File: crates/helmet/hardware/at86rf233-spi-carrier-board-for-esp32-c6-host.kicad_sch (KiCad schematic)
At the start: 23 parts, among them J1 Conn_01x09, U1 AT86RF233-ZU, Y1 16MHz

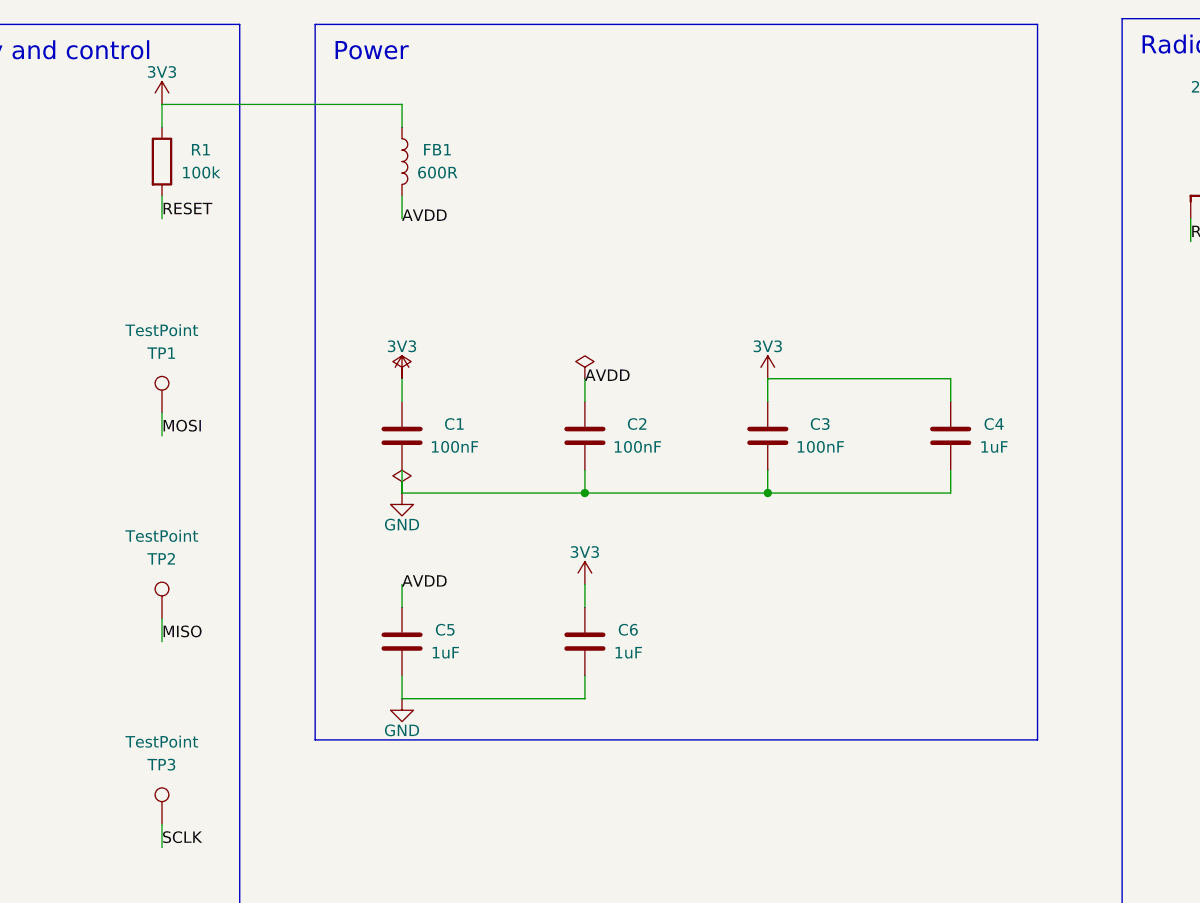
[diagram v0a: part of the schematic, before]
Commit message: copperhead: create pipeline stage: schematic
Created the BOM-consistent AT86RF233 carrier schematic and PINOUT.md. Symbol verification and ERC are clean; legibility has 0 errors and drift is clean.

Verification: ERC clean
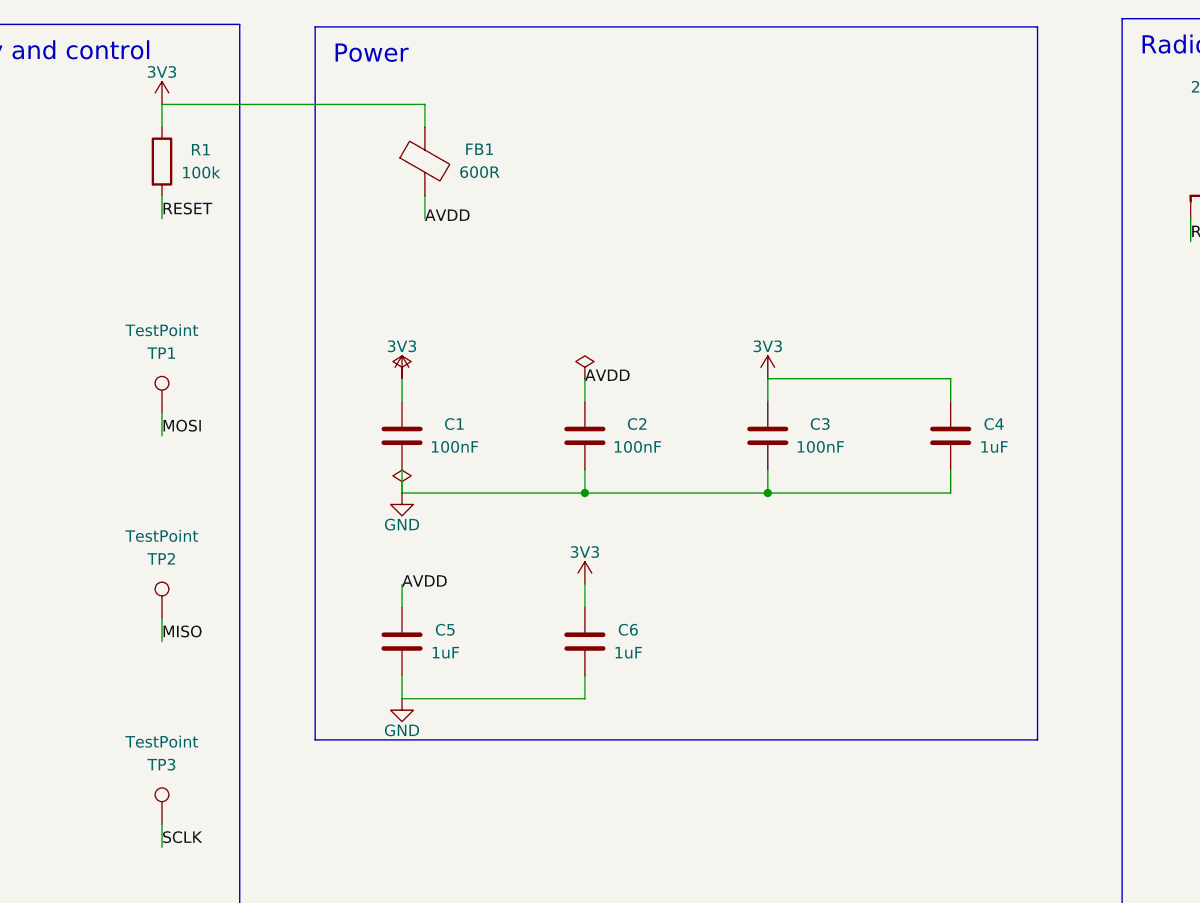
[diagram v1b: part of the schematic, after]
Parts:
- FB1: symbol Device:L -> Device:FerriteBead
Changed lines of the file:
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@@
 	)
 	(wire
-		(pts (xy 134.62 90.17) (xy 134.62 87.63))
-		(stroke (width 0) (type default))
-	)
-	(wire
-		(pts (xy 107.95 87.63) (xy 134.62 87.63))
+		(pts (xy 137.16 90.17) (xy 137.16 87.63))
+		(stroke (width 0) (type default))
+	)
+	(wire
+		(pts (xy 107.95 87.63) (xy 137.16 87.63))
 		(stroke (width 0) (type default))
 	)
@@
 	)
 	(wire
-		(pts (xy 134.62 97.79) (xy 134.62 100.33))
+		(pts (xy 137.16 97.79) (xy 137.16 100.33))
 		(stroke (width 0) (type default))
 	)
@@
 		(fill (type none))
 	)
-	(rectangle (start 124.968 78.74) (end 205.232 158.242)
+	(rectangle (start 124.968 79.0194) (end 205.232 158.242)
 		(stroke (width 0.152) (type solid))
 		(fill (type none))
@@
 		(effects (font (size 2 2)) (justify left top))
 	)
-	(text "Power" (at 126.968 80.74 0)
+	(text "Power" (at 126.968 81.0194 0)
 		(effects (font (size 2 2)) (justify left top))
 	)
@@
 		(effects (font (size 1.27 1.27)))
 	)
-	(label "AVDD" (at 134.62 100.33 0)
+	(label "AVDD" (at 137.16 100.33 0)
 		(effects (font (size 1.27 1.27)))
 	)
@@
 	)
 	(symbol
-		(lib_id "Device:L")
-		(at 134.62 93.98 0)
-		(unit 1)
-		(exclude_from_sim no)
-		(in_bom yes)
-		(on_board yes)
-		(dnp no)
-		(property "Reference" "FB1" (at 138.5543 92.71 0)
-			(effects (font (size 1.27 1.27)))
-		)
-		(property "Value" "600R" (at 138.5543 95.25 0)
-			(effects (font (size 1.27 1.27)))
-		)
-		(property "Footprint" "Inductor_SMD:L_0402_1005Metric" (at 134.62 93.98 0)
-			(effects (font (size 1.27 1.27)) hide)
-		)
-		(property "Datasheet" "~" (at 134.62 93.98 0)
-			(effects (font (size 1.27 1.27)) hide)
-		)
+		(lib_id "Device:FerriteBead")
+		(at 137.16 93.98 0)
+		(unit 1)
+		(exclude_from_sim no)
+		(in_bom yes)
+		(on_board yes)
+		(dnp no)
+		(property "Reference" "FB1" (at 143.2306 92.6592 0)
+			(effects (font (size 1.27 1.27)))
+		)
+		(property "Value" "600R" (at 143.2306 95.1992 0)
+			(effects (font (size 1.27 1.27)))
+		)
+		(property "Footprint" "Inductor_SMD:L_0402_1005Metric" (at 137.16 93.98 0)
+			(effects (font (size 1.27 1.27)) hide)
+		)
+		(property "Datasheet" "~" (at 137.16 93.98 0)
+			(effects (font (size 1.27 1.27)) hide)
+		)

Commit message: prepare AT86RF233 carrier for PCB layout
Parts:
- AE1: footprint Antenna:Antennas_Chip_2.4GHz -> RF_Antenna:Johanson_2450AT18x100
- TP1, TP2, TP3, TP4, TP5: footprint Connector_PinHeader_1.00mm:PinHeader_1x01_P1.00mm_Vertical -> TestPoint:TestPoint_Keystone_5015_Micro_Mini
- U1: footprint Package_DFN_QFN:QFN-32-1EP_5x5mm_P0.5mm_EP3.35x3.35mm -> Package_DFN_QFN:QFN-32-1EP_5x5mm_P0.5mm_EP3.3x3.3mm
- Y1: footprint Crystal:Crystal_SMD_3225-4Pin_3.2x2.5mm -> Crystal:Crystal_SMD_Abracon_ABM8G-4Pin_3.2x2.5mm
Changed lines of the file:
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@@
 	)
 	(symbol
-		(lib_id "power:PWR_FLAG")
+		(lib_id "copperhead_power:PWR_FLAG")
 		(at 134.62 118.11 0)
 		(unit 1)
@@
 	)
 	(symbol
-		(lib_id "power:PWR_FLAG")
+		(lib_id "copperhead_power:PWR_FLAG")
 		(at 154.94 118.11 0)
 		(unit 1)
@@
 	)
 	(symbol
-		(lib_id "power:PWR_FLAG")
+		(lib_id "copperhead_power:PWR_FLAG")
 		(at 134.62 130.81 0)
 		(unit 1)
@@
 	)
 	(symbol
-		(lib_id "power:+3V3")
+		(lib_id "copperhead_power:3V3")
 		(at 107.95 87.63 0)
 		(unit 1)
@@
 	)
 	(symbol
-		(lib_id "power:+3V3")
+		(lib_id "copperhead_power:3V3")
 		(at 175.26 118.11 0)
 		(unit 1)
@@
 	)
 	(symbol
-		(lib_id "power:+3V3")
+		(lib_id "copperhead_power:3V3")
 		(at 134.62 118.11 0)
 		(unit 1)
@@
 	)
 	(symbol
-		(lib_id "power:+3V3")
+		(lib_id "copperhead_power:3V3")
 		(at 154.94 140.97 0)
 		(unit 1)
@@
 	)
 	(symbol
-		(lib_id "power:+3V3")
+		(lib_id "copperhead_power:3V3")
 		(at 69.85 92.71 0)
 		(unit 1)
@@
 	)
 	(symbol
-		(lib_id "power:+3V3")
+		(lib_id "copperhead_power:3V3")
 		(at 303.53 111.76 0)
 		(unit 1)
@@
 	)
 	(symbol
-		(lib_id "power:+3V3")
+		(lib_id "copperhead_power:3V3")
 		(at 295.91 111.76 0)
 		(unit 1)
@@
 		)
 	)
-	(label "AVDD" (at 154.94 118.11 0)
-		(effects (font (size 1.27 1.27)))
-	)
-	(label "AVDD" (at 134.62 140.97 0)
-		(effects (font (size 1.27 1.27)))
-	)
-	(label "AVDD" (at 137.16 100.33 0)
-		(effects (font (size 1.27 1.27)))
-	)
-	(label "AVDD" (at 300.99 109.22 0)
-		(effects (font (size 1.27 1.27)))
-	)
-	(symbol
-		(lib_id "power:GND")
+	(symbol
+		(lib_id "copperhead_power:AVDD")
+		(at 154.94 118.11 0)
+		(unit 1)
+		(exclude_from_sim no)
+		(in_bom yes)
+		(on_board yes)
+		(dnp no)
+		(property "Reference" "#PWR08" (at 154.94 118.11 0)
+			(effects (font (size 1.27 1.27)) hide)
+		)
+		(property "Value" "AVDD" (at 154.94 114.554 0)
+			(effects (font (size 1.27 1.27)))
+		)
+		(property "Footprint" "" (at 154.94 118.11 0)
+			(effects (font (size 1.27 1.27)) hide)
+		)
+		(property "Datasheet" "~" (at 154.94 118.11 0)
+			(effects (font (size 1.27 1.27)) hide)
+		)
+		(pin "1")
+		(instances
+			(project "at86rf233-spi-carrier-board-for-esp32-c6-host"
+				(path "/25b94891-2cac-5fa8-bbe5-b66da5374efa" (reference "#PWR08") (unit 1))
+			)
+		)
+	)
+	(symbol
+		(lib_id "copperhead_power:AVDD")
+		(at 134.62 140.97 0)
+		(unit 1)
+		(exclude_from_sim no)
+		(in_bom yes)
+		(on_board yes)
+		(dnp no)
+		(property "Reference" "#PWR09" (at 134.62 140.97 0)
+			(effects (font (size 1.27 1.27)) hide)
+		)
+		(property "Value" "AVDD" (at 134.62 137.414 0)
+			(effects (font (size 1.27 1.27)))
+		)
+		(property "Footprint" "" (at 134.62 140.97 0)
+			(effects (font (size 1.27 1.27)) hide)
+		)
+		(property "Datasheet" "~" (at 134.62 140.97 0)
+			(effects (font (size 1.27 1.27)) hide)
+		)
+		(pin "1")
+		(instances
+			(project "at86rf233-spi-carrier-board-for-esp32-c6-host"
+				(path "/25b94891-2cac-5fa8-bbe5-b66da5374efa" (reference "#PWR09") (unit 1))
+			)
+		)
+	)
+	(symbol
+		(lib_id "copperhead_power:AVDD")
+		(at 137.16 100.33 0)
+		(unit 1)
+		(exclude_from_sim no)
+		(in_bom yes)
+		(on_board yes)
+		(dnp no)
+		(property "Reference" "#PWR10" (at 137.16 100.33 0)
+			(effects (font (size 1.27 1.27)) hide)
+		)
+		(property "Value" "AVDD" (at 137.16 103.886 0)
+			(effects (font (size 1.27 1.27)))
+		)
+		(property "Footprint" "" (at 137.16 100.33 0)
+			(effects (font (size 1.27 1.27)) hide)
+		)
+		(property "Datasheet" "~" (at 137.16 100.33 0)
+			(effects (font (size 1.27 1.27)) hide)
+		)
+		(pin "1")
+		(instances
+			(project "at86rf233-spi-carrier-board-for-esp32-c6-host"
+				(path "/25b94891-2cac-5fa8-bbe5-b66da5374efa" (reference "#PWR10") (unit 1))
+			)
+		)
+	)
+	(symbol
+		(lib_id "copperhead_power:AVDD")
+		(at 300.99 109.22 0)
+		(unit 1)
+		(exclude_from_sim no)
+		(in_bom yes)
+		(on_board yes)
+		(dnp no)
+		(property "Reference" "#PWR11" (at 300.99 109.22 0)
+			(effects (font (size 1.27 1.27)) hide)
+		)
+		(property "Value" "AVDD" (at 300.99 105.664 0)
+			(effects (font (size 1.27 1.27)))
+		)
+		(property "Footprint" "" (at 300.99 109.22 0)
+			(effects (font (size 1.27 1.27)) hide)
+		)
+		(property "Datasheet" "~" (at 300.99 109.22 0)
+			(effects (font (size 1.27 1.27)) hide)
+		)
+		(pin "1")
+		(instances
+			(project "at86rf233-spi-carrier-board-for-esp32-c6-host"
+				(path "/25b94891-2cac-5fa8-bbe5-b66da5374efa" (reference "#PWR11") (unit 1))
+			)
+		)
+	)
+	(symbol
+		(lib_id "copperhead_power:GND")
 		(at 134.62 130.81 0)
 		(unit 1)
@@
 	)
 	(symbol
-		(lib_id "power:GND")
+		(lib_id "copperhead_power:GND")
 		(at 134.62 153.67 0)
 		(unit 1)
@@
 	)
 	(symbol
-		(lib_id "power:GND")
+		(lib_id "copperhead_power:GND")
 		(at 226.06 128.27 0)
 		(unit 1)
@@
 	)
 	(symbol
-		(lib_id "power:GND")
+		(lib_id "copperhead_power:GND")
 		(at 226.06 151.13 0)
 		(unit 1)
@@
 	)
 	(symbol
-		(lib_id "power:GND")
+		(lib_id "copperhead_power:GND")
 		(at 226.06 173.99 0)
 		(unit 1)
@@
 	)
 	(symbol
-		(lib_id "power:GND")
+		(lib_id "copperhead_power:GND")
 		(at 257.81 99.06 0)
 		(unit 1)
@@
 	)
 	(symbol
-		(lib_id "power:GND")
+		(lib_id "copperhead_power:GND")
 		(at 69.85 95.25 0)
 		(unit 1)
@@
 	)
 	(symbol
-		(lib_id "power:GND")
+		(lib_id "copperhead_power:GND")
 		(at 295.91 162.56 0)
 		(unit 1)
@@
 	)
 	(symbol
-		(lib_id "power:GND")
+		(lib_id "copperhead_power:GND")
 		(at 298.45 162.56 0)
 		(unit 1)
@@
 	)
 	(symbol
-		(lib_id "power:GND")
+		(lib_id "copperhead_power:GND")
 		(at 300.99 162.56 0)
 		(unit 1)
@@
 	)
 	(symbol
-		(lib_id "power:GND")
+		(lib_id "copperhead_power:GND")
 		(at 339.09 125.73 0)
 		(unit 1)
@@
 			(effects (font (size 1.27 1.27)))
 		)
-		(property "Footprint" "Antenna:Antennas_Chip_2.4GHz" (at 224.79 97.79 0)
+		(property "Footprint" "RF_Antenna:Johanson_2450AT18x100" (at 224.79 97.79 0)
 			(effects (font (size 1.27 1.27)) hide)
 		)
@@
 			(effects (font (size 1.27 1.27)))
 		)
-		(property "Footprint" "Connector_PinHeader_1.00mm:PinHeader_1x01_P1.00mm_Vertical" (at 107.95 121.92 0)
+		(property "Footprint" "TestPoint:TestPoint_Keystone_5015_Micro_Mini" (at 107.95 121.92 0)
 			(effects (font (size 1.27 1.27)) hide)
 		)
@@
 			(effects (font (size 1.27 1.27)))
 		)
-		(property "Footprint" "Connector_PinHeader_1.00mm:PinHeader_1x01_P1.00mm_Vertical" (at 107.95 144.78 0)
+		(property "Footprint" "TestPoint:TestPoint_Keystone_5015_Micro_Mini" (at 107.95 144.78 0)
 			(effects (font (size 1.27 1.27)) hide)
 		)
@@
 			(effects (font (size 1.27 1.27)))
 		)
-		(property "Footprint" "Connector_PinHeader_1.00mm:PinHeader_1x01_P1.00mm_Vertical" (at 107.95 167.64 0)
+		(property "Footprint" "TestPoint:TestPoint_Keystone_5015_Micro_Mini" (at 107.95 167.64 0)
 			(effects (font (size 1.27 1.27)) hide)
 		)
@@
 			(effects (font (size 1.27 1.27)))
 		)
-		(property "Footprint" "Connector_PinHeader_1.00mm:PinHeader_1x01_P1.00mm_Vertical" (at 107.95 190.5 0)
+		(property "Footprint" "TestPoint:TestPoint_Keystone_5015_Micro_Mini" (at 107.95 190.5 0)
 			(effects (font (size 1.27 1.27)) hide)
 		)
@@
 			(effects (font (size 1.27 1.27)))
 		)
-		(property "Footprint" "Connector_PinHeader_1.00mm:PinHeader_1x01_P1.00mm_Vertical" (at 339.09 96.52 0)
+		(property "Footprint" "TestPoint:TestPoint_Keystone_5015_Micro_Mini" (at 339.09 96.52 0)
 			(effects (font (size 1.27 1.27)) hide)
 		)
@@
 			(effects (font (size 1.27 1.27)))
 		)
-		(property "Footprint" "Package_DFN_QFN:QFN-32-1EP_5x5mm_P0.5mm_EP3.35x3.35mm" (at 298.45 137.16 0)
+		(property "Footprint" "Package_DFN_QFN:QFN-32-1EP_5x5mm_P0.5mm_EP3.3x3.3mm" (at 298.45 137.16 0)
 			(effects (font (size 1.27 1.27)) hide)
 		)
@@
 			(effects (font (size 1.27 1.27)))
 		)
-		(property "Footprint" "Crystal:Crystal_SMD_3225-4Pin_3.2x2.5mm" (at 339.09 118.11 0)
-			(effects (font (size 1.27 1.27)) hide)
-		)
+		(property "Footprint" "Crystal:Crystal_SMD_Abracon_ABM8G-4Pin_3.2x2.5mm" (at 339.09 118.11 0)
+			(effects (font (size 1.27 1.27)) hide)
+		)

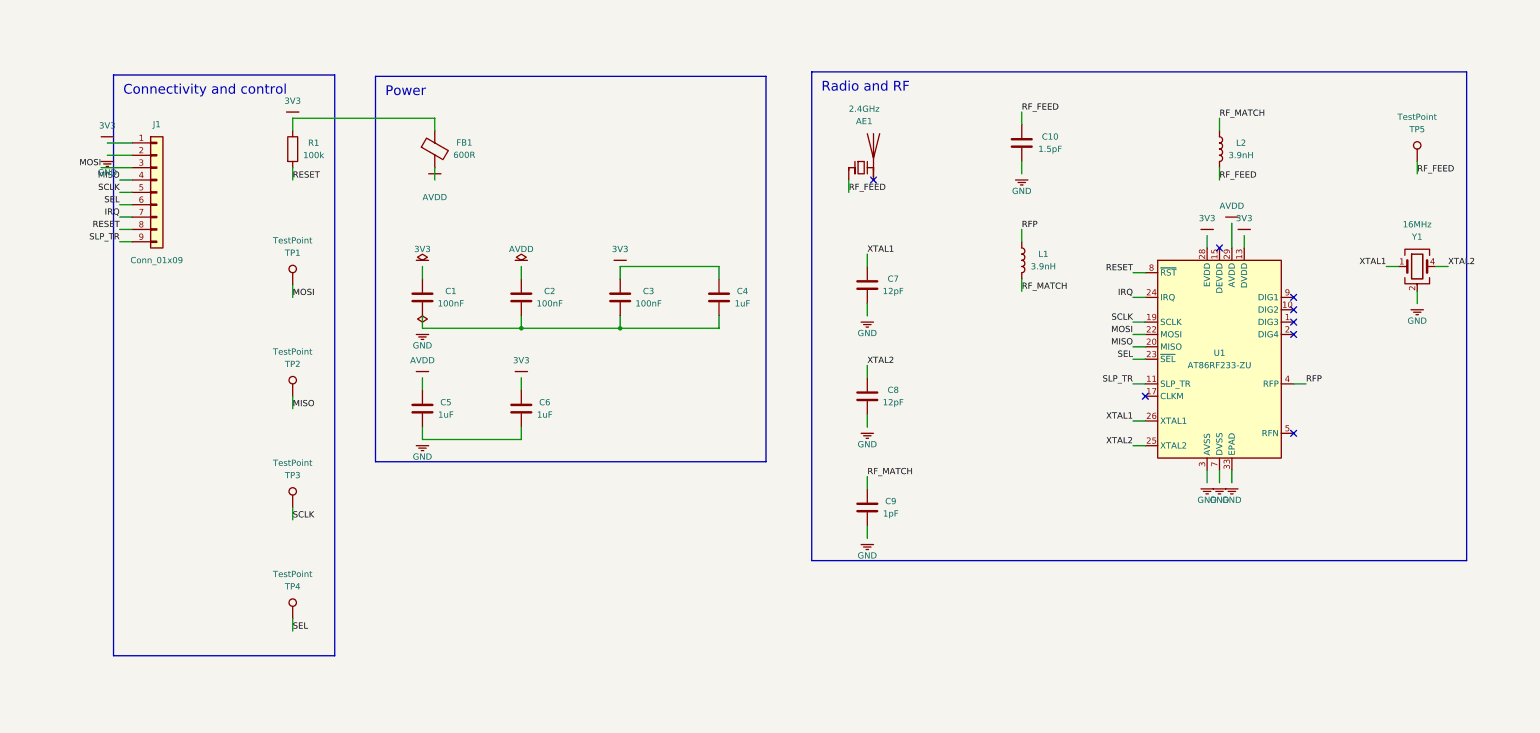
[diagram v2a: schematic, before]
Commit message: copperhead: create pipeline stage: part-selection
Created docs/BOM.md in the required fixed format with one row per refdes, value-only Value cells, UNVERIFIED sourceable MPN candidates, and per-part power/leakage rationale. Confirmed installed symbols and authoritative pins for U1, B1, J1, Y1, AE1, FB1, and test points. Reconciled the pre-existing schematic drift by adding B1 and C11/C12 so RFP and RFN each couple through 22 pF C0G capacitors into the balun. Updated PINOUT, decisions, changelog, and intent. ERC is clean, all 14 source-library symbols verify, legibility has zero errors (two advisories), and documentation drift is clean.

Verification: ERC clean
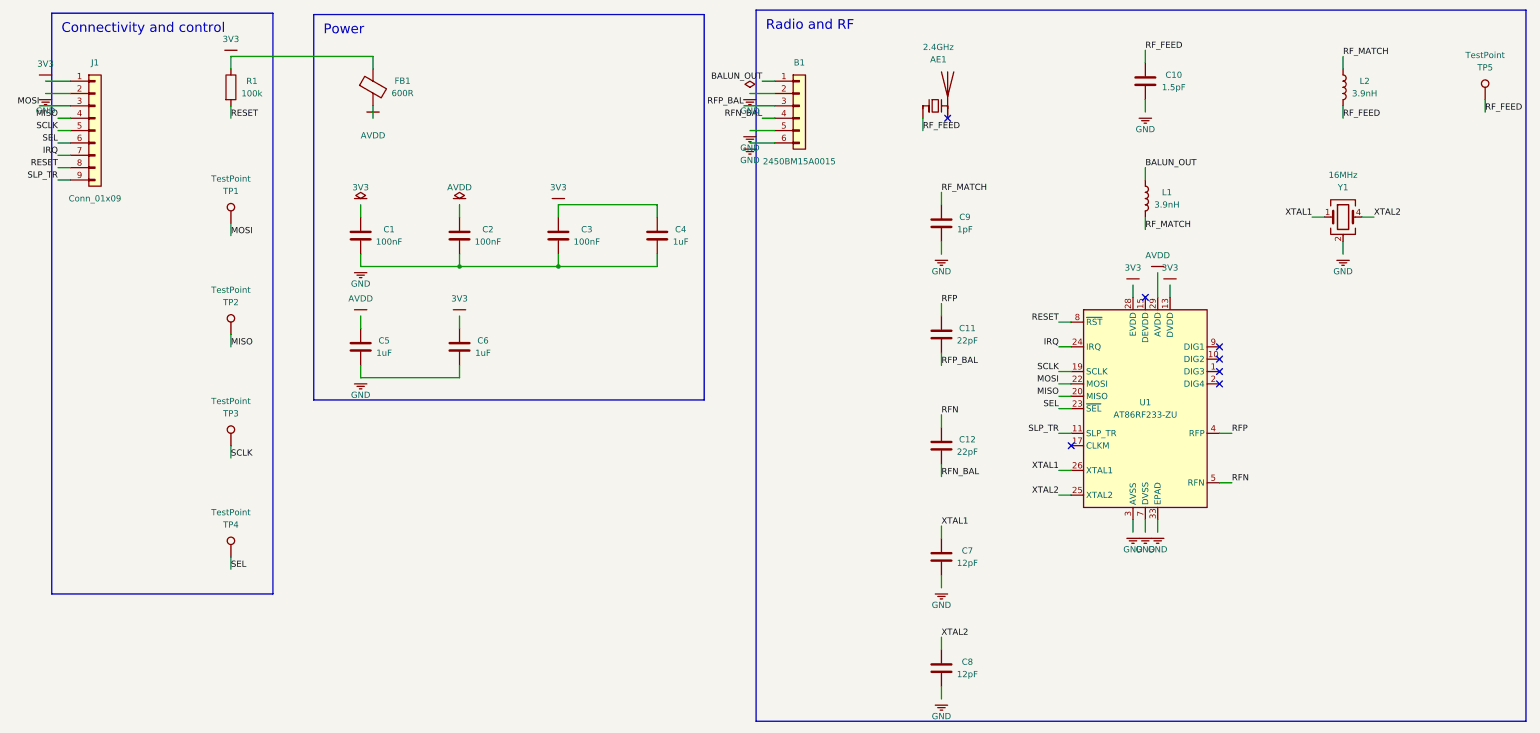
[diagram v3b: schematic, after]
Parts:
- added B1: 2450BM15A0015, ciu:Johanson_2450BM15A0015, symbol Connector_Generic:Conn_01x06
- added C11, C12: 22pF, Capacitor_SMD:C_0402_1005Metric, symbol Device:C
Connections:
- net GND: now also B1.2 (Pin_2), B1.5 (Pin_5), B1.6 (Pin_6)
- net RFP: now also C11.1; no longer L1.1
- net RFN: now reaches U1.5 (RFN)
- net RFN: now also C12.1
- new net BALUN_OUT: B1.1 (Pin_1), L1.1
- new net RFN_BAL: B1.4 (Pin_4), C12.2
- new net RFP_BAL: B1.3 (Pin_3), C11.2
- no-connect marks 8 -> 7
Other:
- moved on the sheet: AE1, C1, C10, C2, C3, C4, C5, C6, C7, C8, C9, FB1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
